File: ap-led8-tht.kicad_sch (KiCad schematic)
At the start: 10 parts, among them J1 Conn_01x08_Socket, J2 Conn_01x08_Socket

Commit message: Initial PCB
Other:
- moved on the sheet: D0, D1, D2, D3, D4, D5, D6, D7, J1, J2

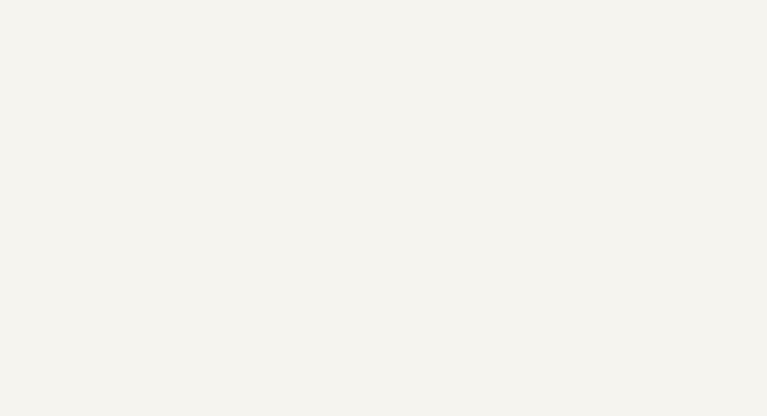
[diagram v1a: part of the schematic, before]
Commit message: schematic: add oshw logo and certification mark
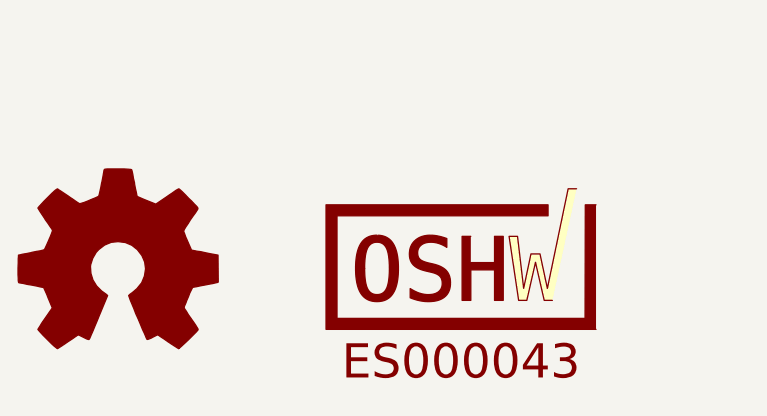
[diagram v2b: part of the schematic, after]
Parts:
- added LOGO2: ~, symbol OSHW_Certification_Mark:OSHW_Certification_Mark_Stacked_Large
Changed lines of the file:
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@@
+    )
+  )
+  (symbol (lib_id "OSHW_Certification_Mark:OSHW_Certification_Mark_Stacked_Large") (at 68.58 119.38 0) (unit 1)
+    (in_bom no) (on_board no) (dnp no) (fields_autoplaced)
+    (property "Reference" "LOGO2" (at 68.58 119.38 0)
+      (effects (font (size 1.27 1.27)) hide)
+    )
+    (property "Value" "~" (at 68.58 119.38 0)
+      (effects (font (size 1.27 1.27)) hide)
+    )
+    (property "Footprint" "" (at 68.58 119.38 0)
+      (effects (font (size 1.27 1.27)) hide)
+    )
+    (property "Datasheet" "" (at 68.58 119.38 0)
+      (effects (font (size 1.27 1.27)) hide)
+    )
+    (instances
+      (project "ap-led8-tht"
+        (path "/9d21c3cd-8861-458d-b3e8-c0eff0bcbaa3"
+          (reference "LOGO2") (unit 1)
+        )
+      )
     )
   )
@@
         )
       )
+    )
+  )
+  (symbol (lib_id "Graphic:Logo_Open_Hardware_Large") (at 30.48 120.65 0) (unit 1)
+    (in_bom no) (on_board no) (dnp no) (fields_autoplaced)
+    (property "Reference" "#SYM1" (at 30.48 107.95 0)
+      (effects (font (size 1.27 1.27)) hide)
+    )
+    (property "Value" "Logo_Open_Hardware_Large" (at 30.48 130.81 0)
+      (effects (font (size 1.27 1.27)) hide)
+    )
+    (property "Footprint" "" (at 30.48 120.65 0)
+      (effects (font (size 1.27 1.27)) hide)
+    )
+    (property "Datasheet" "~" (at 30.48 120.65 0)
+      (effects (font (size 1.27 1.27)) hide)
+    )
+    (property "Sim.Enable" "0" (at 30.48 120.65 0)
+      (effects (font (size 1.27 1.27)) hide)
+    )
+    (instances
+      (project "ap-led8-tht"
+        (path "/9d21c3cd-8861-458d-b3e8-c0eff0bcbaa3"
+          (reference "#SYM1") (unit 1)
+        )
+      )
